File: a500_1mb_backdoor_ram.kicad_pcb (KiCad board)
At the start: 2 copper layers, 58 x 88.2 mm, 21 parts, among them J1 Expansion, P99 OSHW_LOGO, U1 V53C181608K60, U2 V53C181608K60

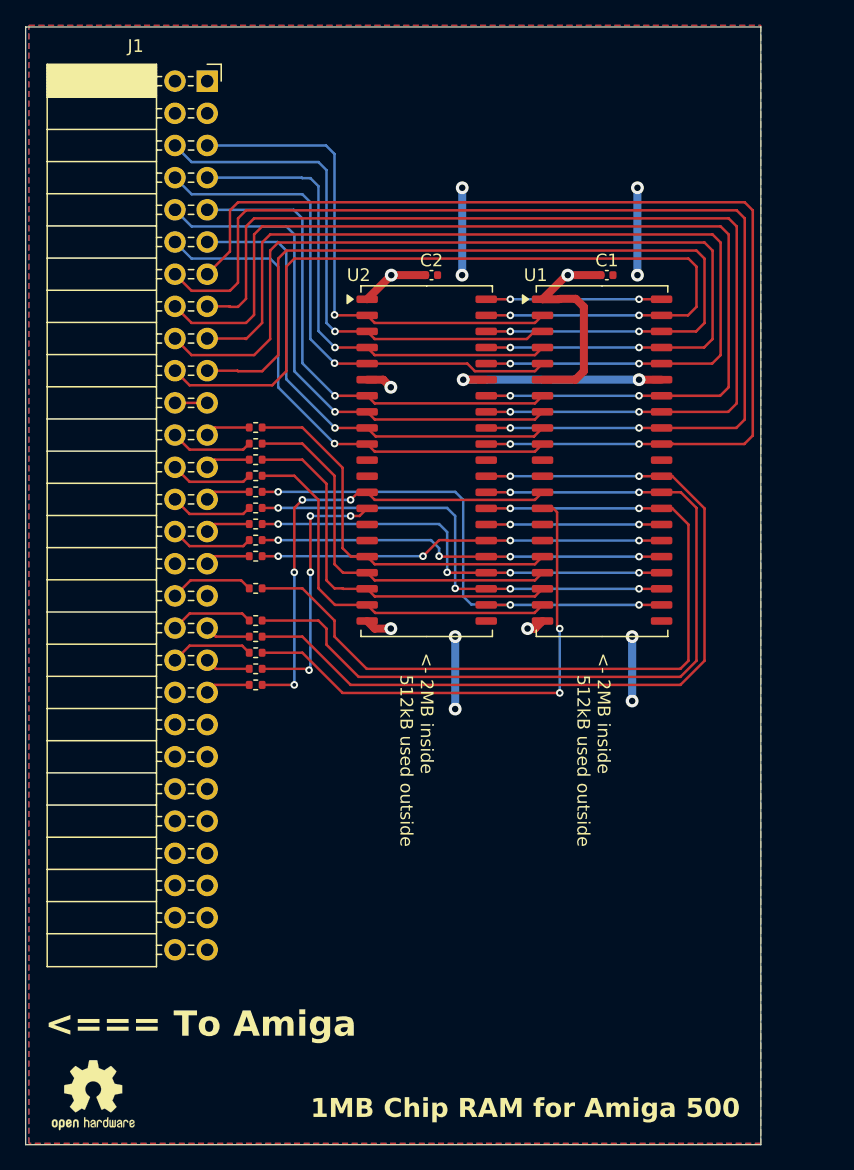
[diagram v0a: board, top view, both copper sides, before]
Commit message: Version 2.0 - fixing GND vs. VDD connection
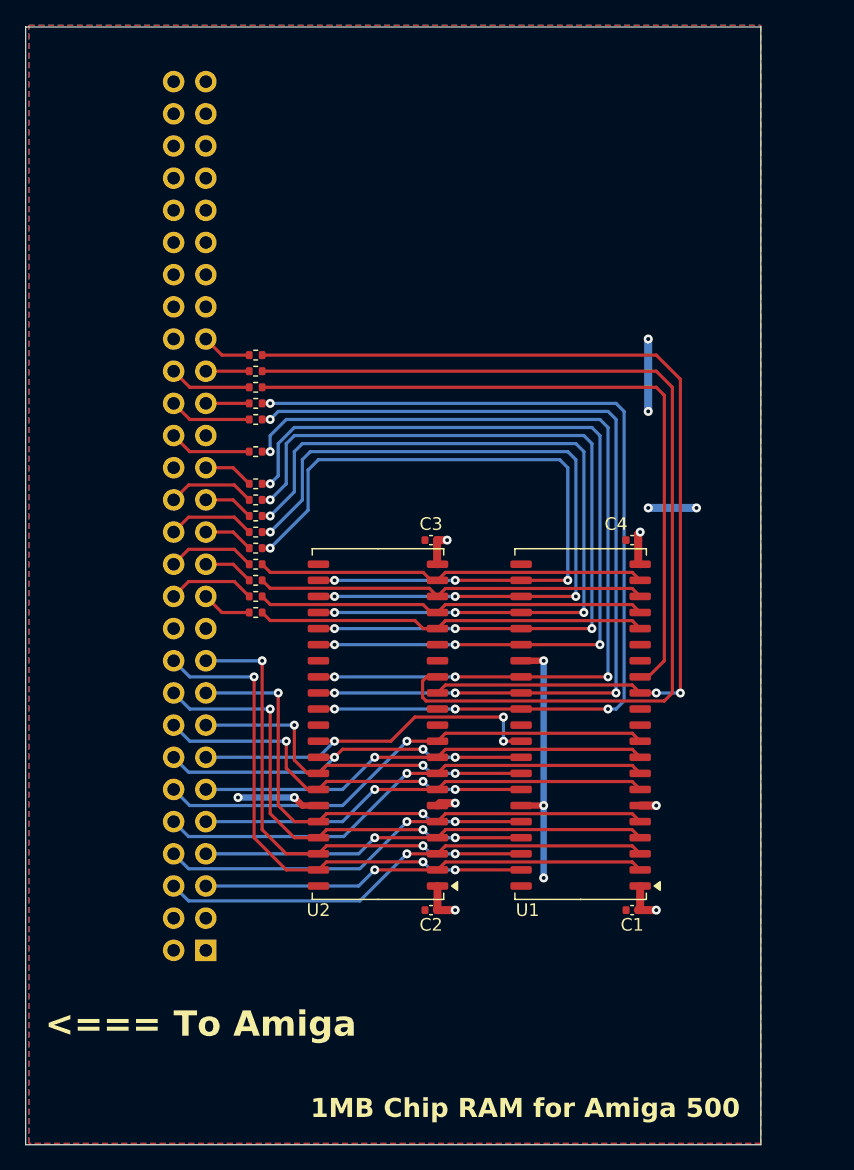
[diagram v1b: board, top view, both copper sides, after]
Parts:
- removed P99: OSHW_LOGO, Symbol:OSHW-Logo2_7.3x6mm_Copper
- added C3: 100n, Capacitor_SMD:C_0402_1005Metric, F.Cu at (93.3, 80.0)
- added C4: 100n, Capacitor_SMD:C_0402_1005Metric, F.Cu at (109.2, 80.0)
- J1: moved to B.Cu
- moved J1 68.6 mm to (75.6, 112.4)
- moved C1 50.2 mm to (109.2, 109.2), turned to 180 degrees
- moved C2 50.1 mm to (93.3, 109.2), turned to 180 degrees
- moved R13 26.0 mm to (79.5, 65.4)
- moved R16 23.5 mm to (79.5, 66.7)
- moved U2 21.3 mm to (89.2, 94.6), turned to 180 degrees
- moved U1 21.0 mm to (105.2, 94.6), turned to 180 degrees
- moved R11 21.0 mm to (79.5, 67.9)
- moved R15 18.4 mm to (79.5, 69.2)
- moved R10 15.9 mm to (79.5, 70.5)
- moved R1 14.6 mm to (79.5, 85.7)
- moved R2 12.1 mm to (79.5, 84.5)
- moved R9 10.8 mm to (79.5, 73.0)
- moved R3 9.53 mm to (79.5, 83.2)
- moved R4 6.98 mm to (79.5, 81.9)
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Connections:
- J1 pad 21: +5V -> GND
- J1 pad 22: +5V -> GND
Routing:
- net /~{RAS1}: track 20.7 -> 79.7 mm, vias 4 -> 0
- net /D8: track 87.6 -> 29.4 mm, vias 2 -> 3
- net /D9: track 88.0 -> 30.2 mm, vias 2 -> 3
- net /D10: track 82.3 -> 28.6 mm, vias 2 -> 3
- net /D11: track 82.9 -> 31.3 mm, vias 2 -> 3
- net /~{W}: track 37.1 -> 78.3 mm, vias 4 -> 2
- net /D12: track 75.6 -> 34.8 mm, vias 2 -> 3
- net /D13: track 76.2 -> 37.5 mm, vias 2 -> 3
- net /A8: track 32.1 -> 69.0 mm
- net /A7: track 32.4 -> 66.5 mm
- net GND: track 70.2 -> 36.8 mm, vias 14 -> 9
- net /D14: track 70.5 -> 39.5 mm, vias 2 -> 3
- net /D15: track 70.9 -> 42.2 mm, vias 2 -> 3
- net /A6: track 35.0 -> 63.5 mm
- net /A5: track 37.5 -> 60.6 mm
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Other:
- board text removed: "<- 2MB inside 512kB used outside"
